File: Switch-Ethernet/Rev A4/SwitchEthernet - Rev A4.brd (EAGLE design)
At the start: 86 x 90 mm, 118 parts, among them J1 22-05-7028-02, J2 DF17(2.0)-20DP-0.5V(57), J3 DF17(4.0)-20DP-0.5V(57), P1 RB1-125BAG1A, T1 H1102FNL, T2 H1102FNL, U1 TC1264-3.3, U2 TC1264-1.8, U3 KSZ8995MA, U4 AT24C02C-SSHM-B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

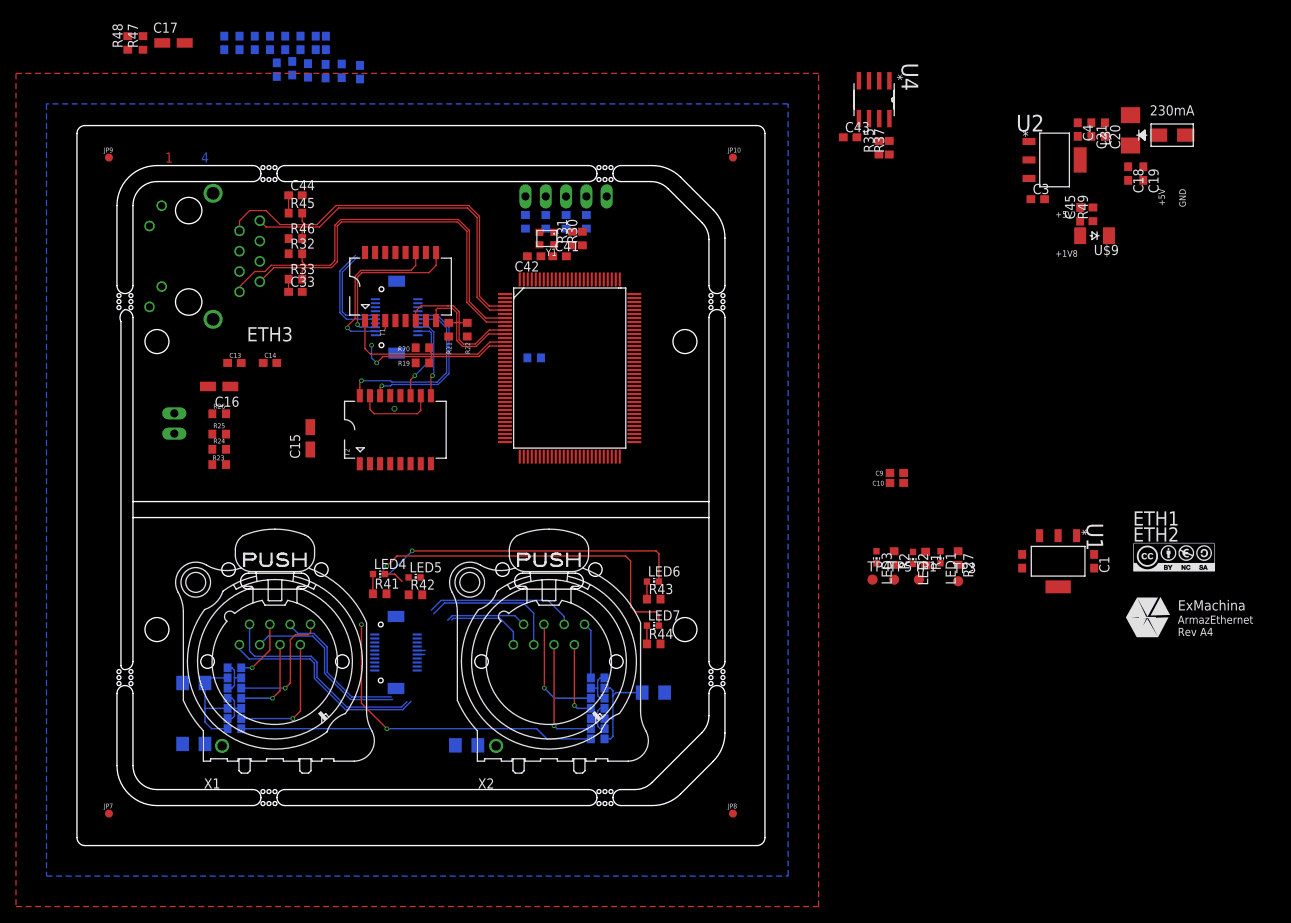
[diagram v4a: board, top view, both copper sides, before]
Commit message: Reroute ETH signals
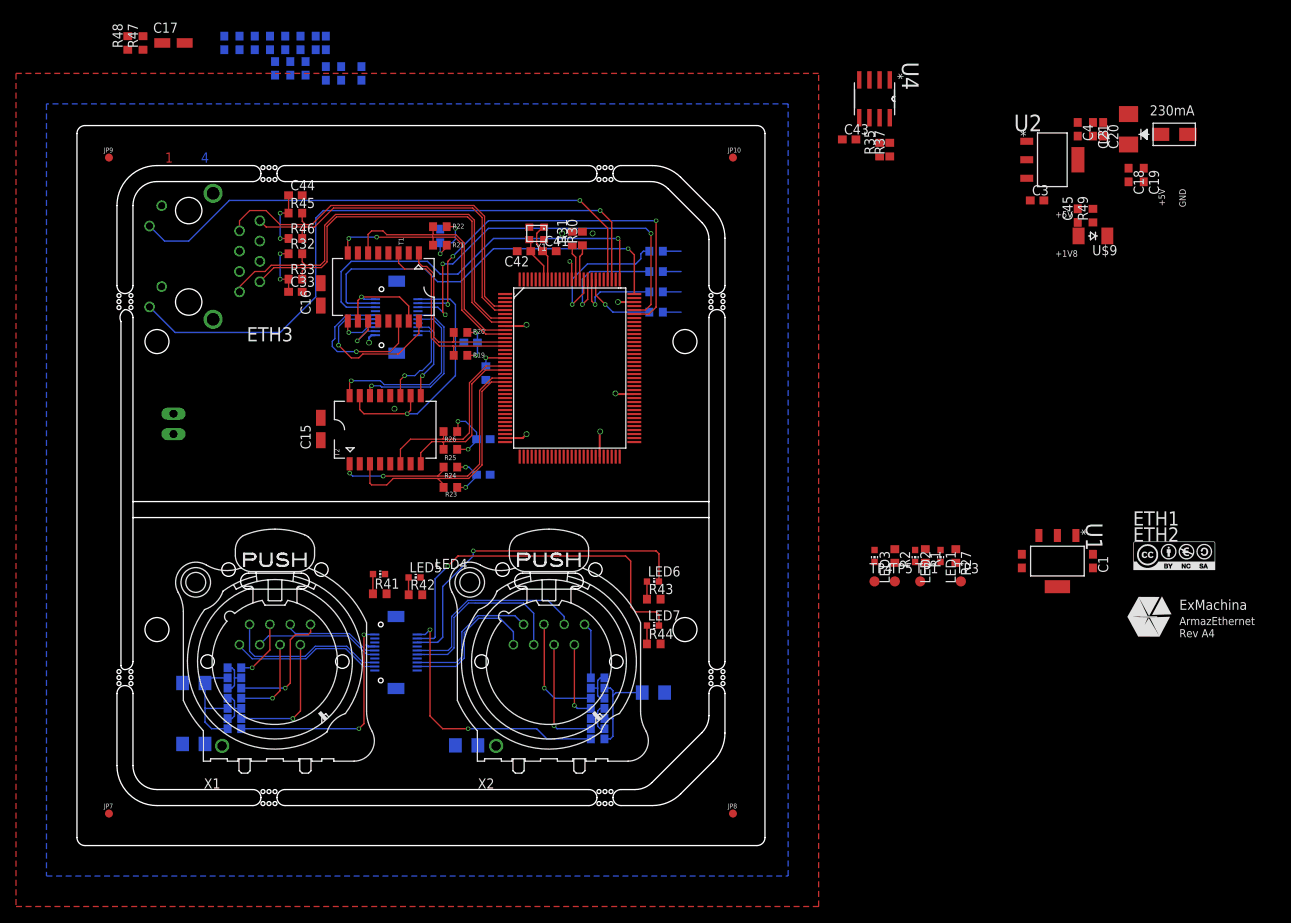
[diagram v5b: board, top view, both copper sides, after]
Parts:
- removed JP1: (no value), pinhead:1X05
- moved C10 64.9 mm to (45.4, 76.2), flipped to the bottom, turned to 90 degrees
- moved C9 55.7 mm to (49.2, 62.9), flipped to the bottom
- moved C13 34.1 mm to (50.8, 46.4), flipped to the bottom, turned to 180 degrees
- moved R23 29.0 mm to (46.7, 44.8), turned to 180 degrees
- moved R24 29.0 mm to (46.7, 47.3), turned to 180 degrees
- moved R26 29.0 mm to (46.7, 51.8), turned to 180 degrees
- moved R25 29.0 mm to (46.7, 49.5), turned to 180 degrees
- moved C14 28.3 mm to (50.8, 50.8), flipped to the bottom
- moved R39 19.9 mm to (72.4, 66.7), turned to 180 degrees
- moved C16 17.1 mm to (30.5, 68.9), turned to 90 degrees
- moved R38 16.3 mm to (72.4, 69.2), turned to 180 degrees
- moved R22 13.3 mm to (45.4, 77.4), turned to 180 degrees
- moved R36 12.9 mm to (72.4, 71.8), turned to 180 degrees
- moved R21 10.6 mm to (45.4, 75.0), turned to 180 degrees
- moved R40 9.45 mm to (72.4, 74.3), turned to 180 degrees
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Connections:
- net GND: no longer JP1.5
- net SCL_CPU: no longer JP1.2
- net SDA_CPU: no longer JP1.3
- net SPIQ_CPU: no longer JP1.1
- net SPIS-N_CPU: no longer JP1.4
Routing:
- net L3-2: track 0.00 -> 78.9 mm, vias 0 -> 1
- net L3-1: track 0.00 -> 68.0 mm, vias 0 -> 1
- net L2-2: track 43.0 -> 97.7 mm, vias 1 -> 4
- net L2-1: track 38.9 -> 92.4 mm, vias 1 -> 4
- net L1-2: track 0.00 -> 51.1 mm, vias 0 -> 1
- net L1-1: track 2.51 -> 51.2 mm, vias 0 -> 1
- net TX2_ISO_P: track 0.00 -> 32.6 mm, vias 0 -> 2
- net TX2_ISO_N: track 0.00 -> 31.6 mm
- net CT_1: track 16.0 -> 41.4 mm, vias 0 -> 3
- net RX2_ISO_P: track 0.00 -> 23.9 mm
- net RX1_N: track 47.7 -> 25.7 mm
- net RX1_P: track 47.0 -> 25.0 mm
- net RX2_ISO_N: track 0.00 -> 21.0 mm
- net SPIS-N: track 0.00 -> 18.4 mm, vias 0 -> 1
- net RX1_ISO_N: track 15.7 -> 32.4 mm, vias 0 -> 2
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
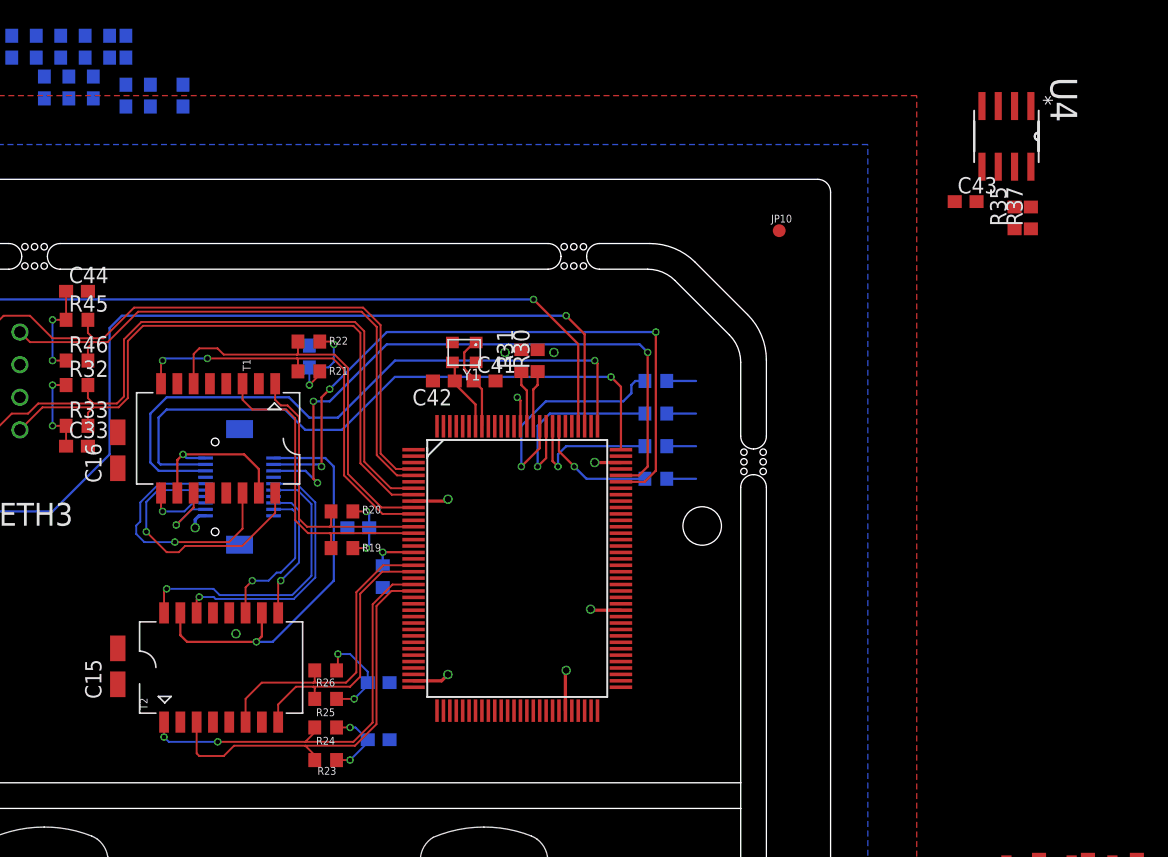
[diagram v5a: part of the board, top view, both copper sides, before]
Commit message: Route the spi nets
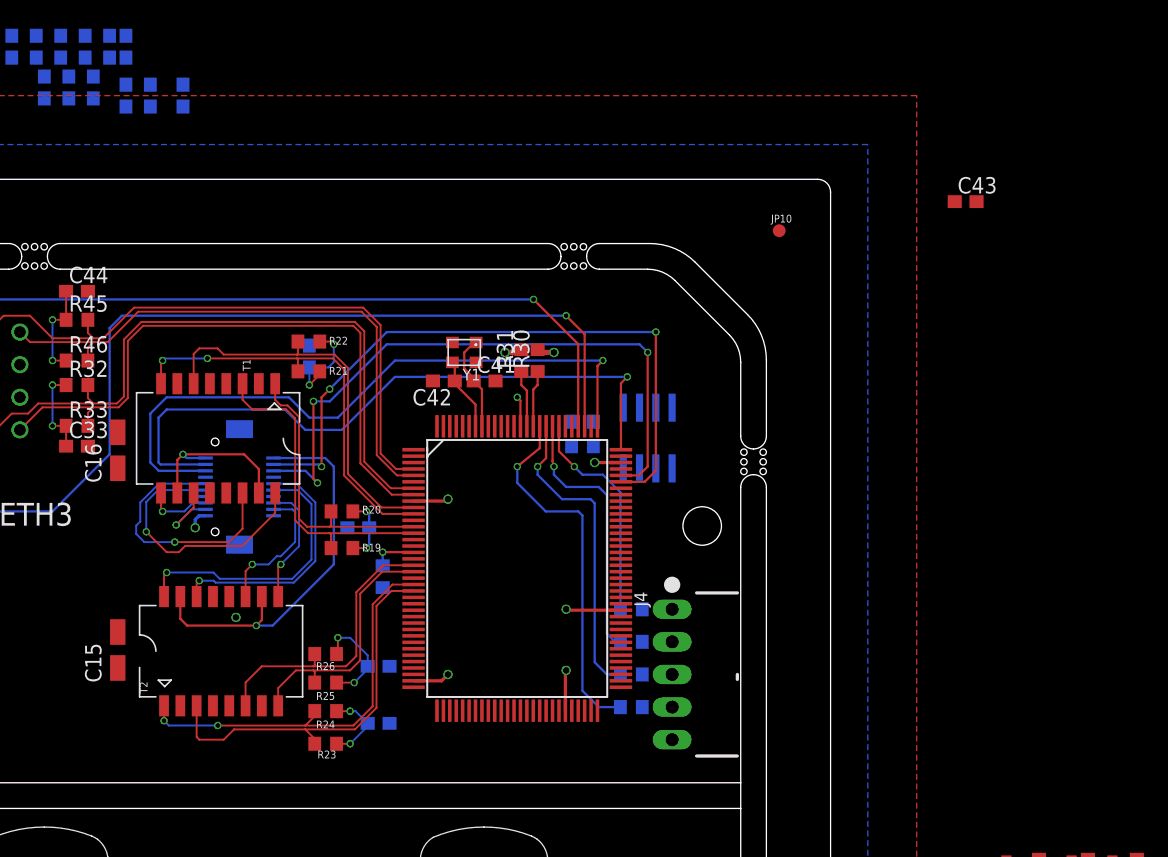
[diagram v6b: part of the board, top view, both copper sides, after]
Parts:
- added J4: 22-05-7058-05, con-molex:7395-05
- moved R37 39.2 mm to (66.7, 69.2), flipped to the bottom, turned to 180 degrees
- moved R35 37.2 mm to (66.7, 71.1), flipped to the bottom, turned to 180 degrees
- moved U4 36.5 mm to (71.8, 69.8), flipped to the bottom
- moved R40 25.5 mm to (70.5, 48.9)
- moved R36 20.4 mm to (70.5, 51.4)
- moved R38 15.4 mm to (70.5, 54.0)
- moved R39 10.3 mm to (70.5, 56.5)
- moved C13 1.27 mm to (50.8, 47.6)
- moved C14 1.27 mm to (50.8, 52.1)
- moved C15 1.27 mm to (30.5, 53.3)
- moved R23 1.27 mm to (46.7, 46.0)
- moved R24 1.27 mm to (46.7, 48.6)
- moved R26 1.27 mm to (46.7, 53.0)
- moved T2 1.27 mm to (38.5, 53.2)
- moved R25 1.27 mm to (46.7, 50.8)
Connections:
- net GND: now also J4.5
- net SCL_CPU: now also J4.2
- net SDA_CPU: now also J4.3
- net SPIQ_CPU: now also J4.1
- net SPIS-N_CPU: now also J4.4
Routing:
- net SPIS-N: track 18.4 -> 28.5 mm
- net SCL: track 11.3 -> 20.7 mm
- net SDA: track 15.3 -> 24.2 mm
- net SPIQ: track 9.53 -> 17.2 mm
- net +3V3: track 14.8 -> 19.4 mm
- net SPIS-N_CPU: track 2.28 -> 0.00 mm
- net SPIQ_CPU: track 2.28 -> 0.00 mm
- net SDA_CPU: track 2.28 -> 0.00 mm
- net SCL_CPU: track 2.28 -> 0.00 mm
- net TX2_N: track 45.8 -> 44.6 mm
- net RX2_ISO_N: track 21.0 -> 19.7 mm
- net TX2_P: track 47.0 -> 45.7 mm
- net TX2_ISO_P: track 32.6 -> 31.4 mm
- net RX2_P: track 30.8 -> 29.6 mm
- net RX2_N: track 28.9 -> 27.6 mm
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
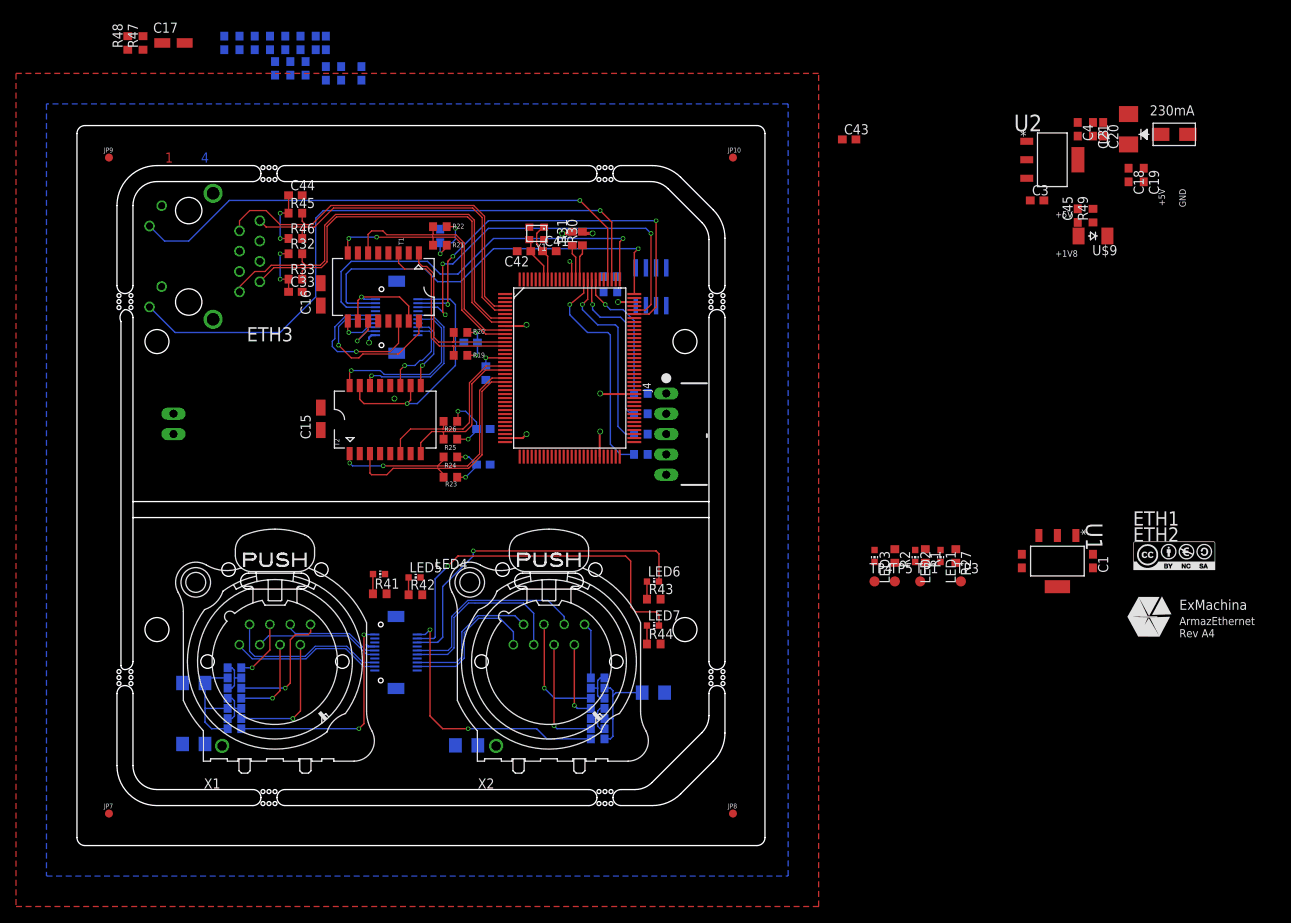
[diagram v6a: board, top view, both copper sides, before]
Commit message: Change to the top the RJ45 connector and re-route it
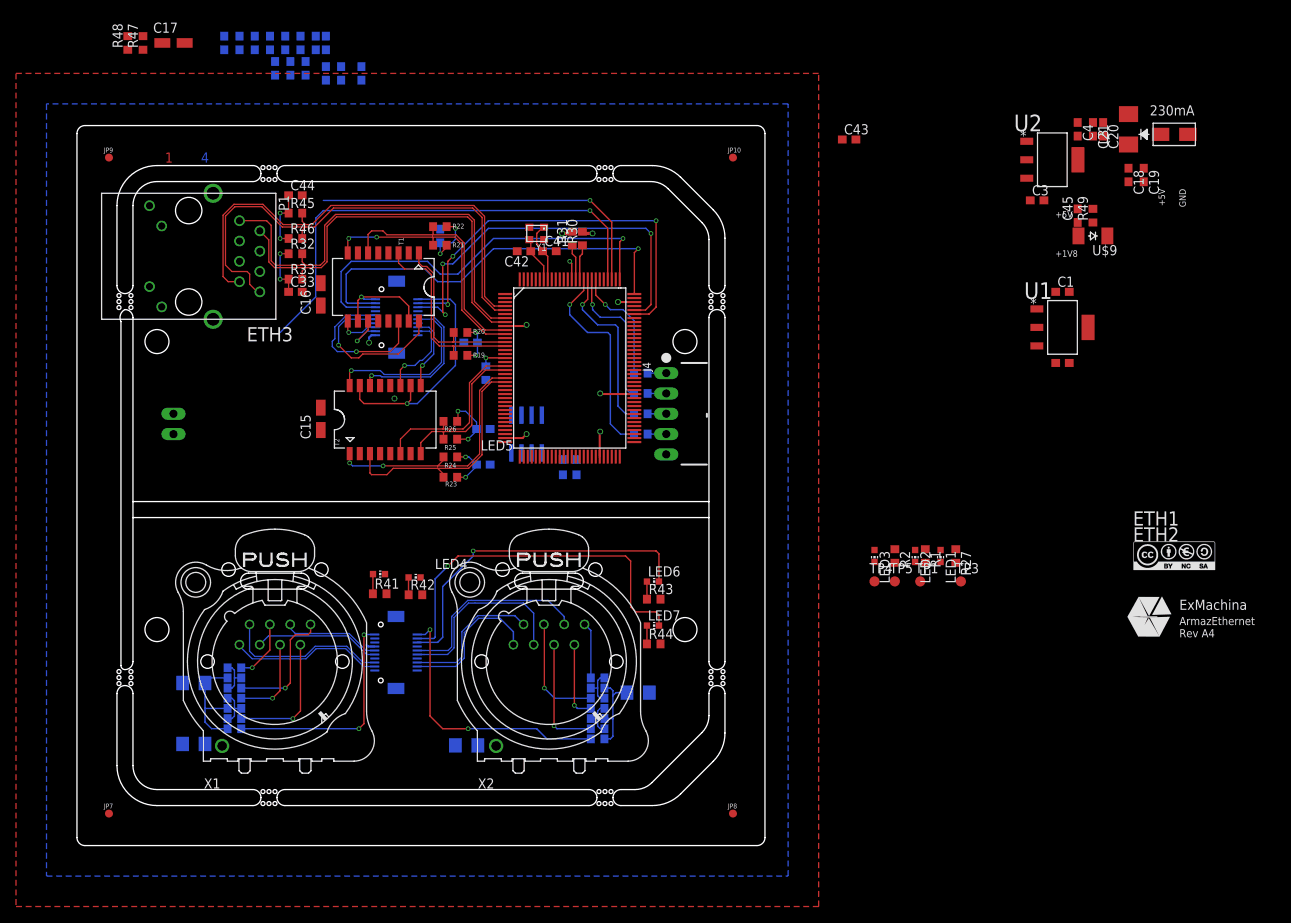
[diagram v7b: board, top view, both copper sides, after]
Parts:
- moved C1 33.9 mm to (123.2, 69.2), turned to 0 degrees
- moved U1 29.2 mm to (123.2, 64.8), turned to 0 degrees
- moved C2 25.3 mm to (123.2, 60.3), turned to 0 degrees
- moved U4 24.1 mm to (56.2, 51.4)
- moved R35 23.4 mm to (61.6, 48.3), turned to 0 degrees
- moved R37 23.4 mm to (61.6, 46.4)
- moved J4 2.54 mm to (73.7, 54.0)
- moved R36 2.54 mm to (70.5, 54.0)
- moved R38 2.54 mm to (70.5, 56.5)
- moved R39 2.54 mm to (70.5, 59.1)
- moved R40 2.54 mm to (70.5, 51.4)
- moved C11 1.91 mm to (70.2, 19.1)
- flipped P1 to the top, turned to 270 degrees
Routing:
- net L3-2: track 78.9 -> 44.3 mm
- net RX3_ISO_N: track 44.7 -> 62.8 mm
- net RX3_ISO_P: track 49.4 -> 60.5 mm
- net L3-1: track 68.0 -> 60.3 mm
- net TX3_ISO_P: track 53.1 -> 56.3 mm
- net TX3_ISO_N: track 49.6 -> 52.4 mm
- net SPIS-N: track 28.5 -> 25.9 mm
- net SPIQ: track 17.2 -> 14.6 mm
- net SDA: track 24.2 -> 21.7 mm
- net SCL: track 20.7 -> 18.2 mm
- net SPIS-N_CPU: track 0.00 -> 2.33 mm
- net SPIQ_CPU: track 0.00 -> 2.33 mm
- net SDA_CPU: track 0.00 -> 2.33 mm
- net SCL_CPU: track 0.00 -> 2.33 mm
- net N$13: track 13.0 -> 11.1 mm
